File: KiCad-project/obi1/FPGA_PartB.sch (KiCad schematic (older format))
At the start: 10 parts, among them U3 XC6SLX16-FTG256

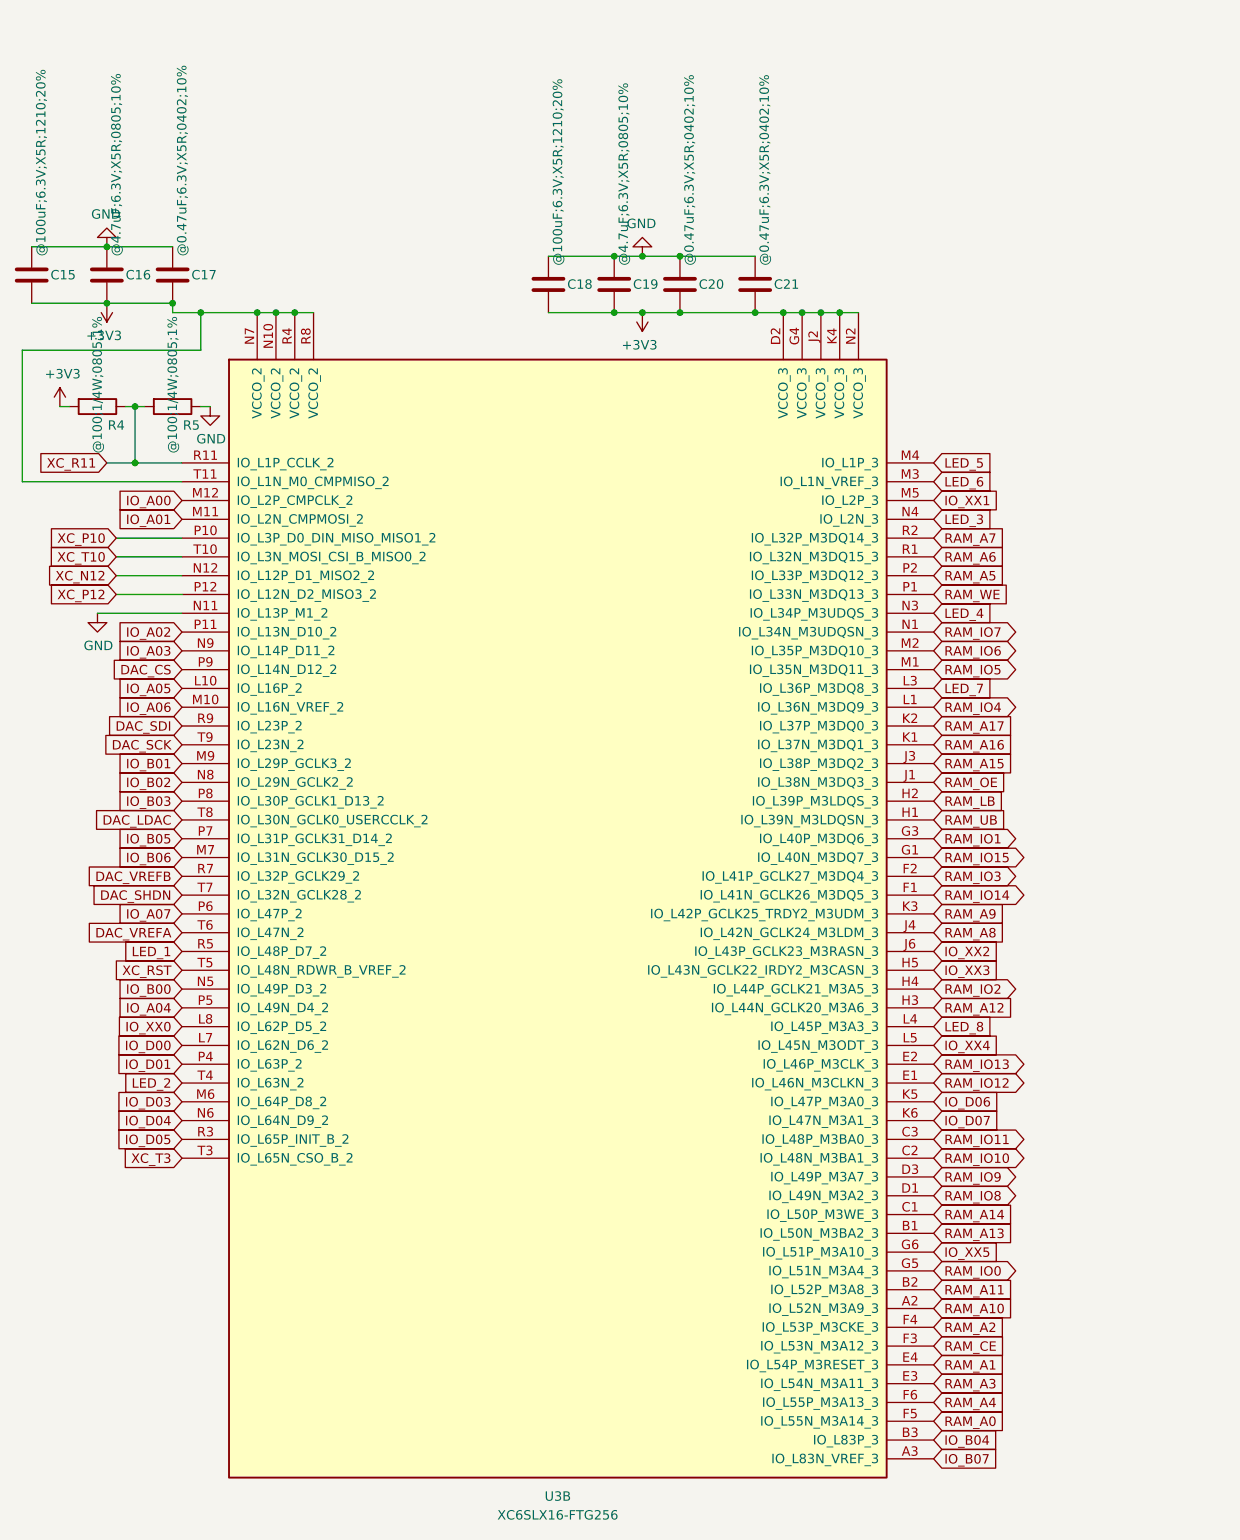
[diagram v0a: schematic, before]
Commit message: Resize board, change layout, re-route IO pins, new imu added
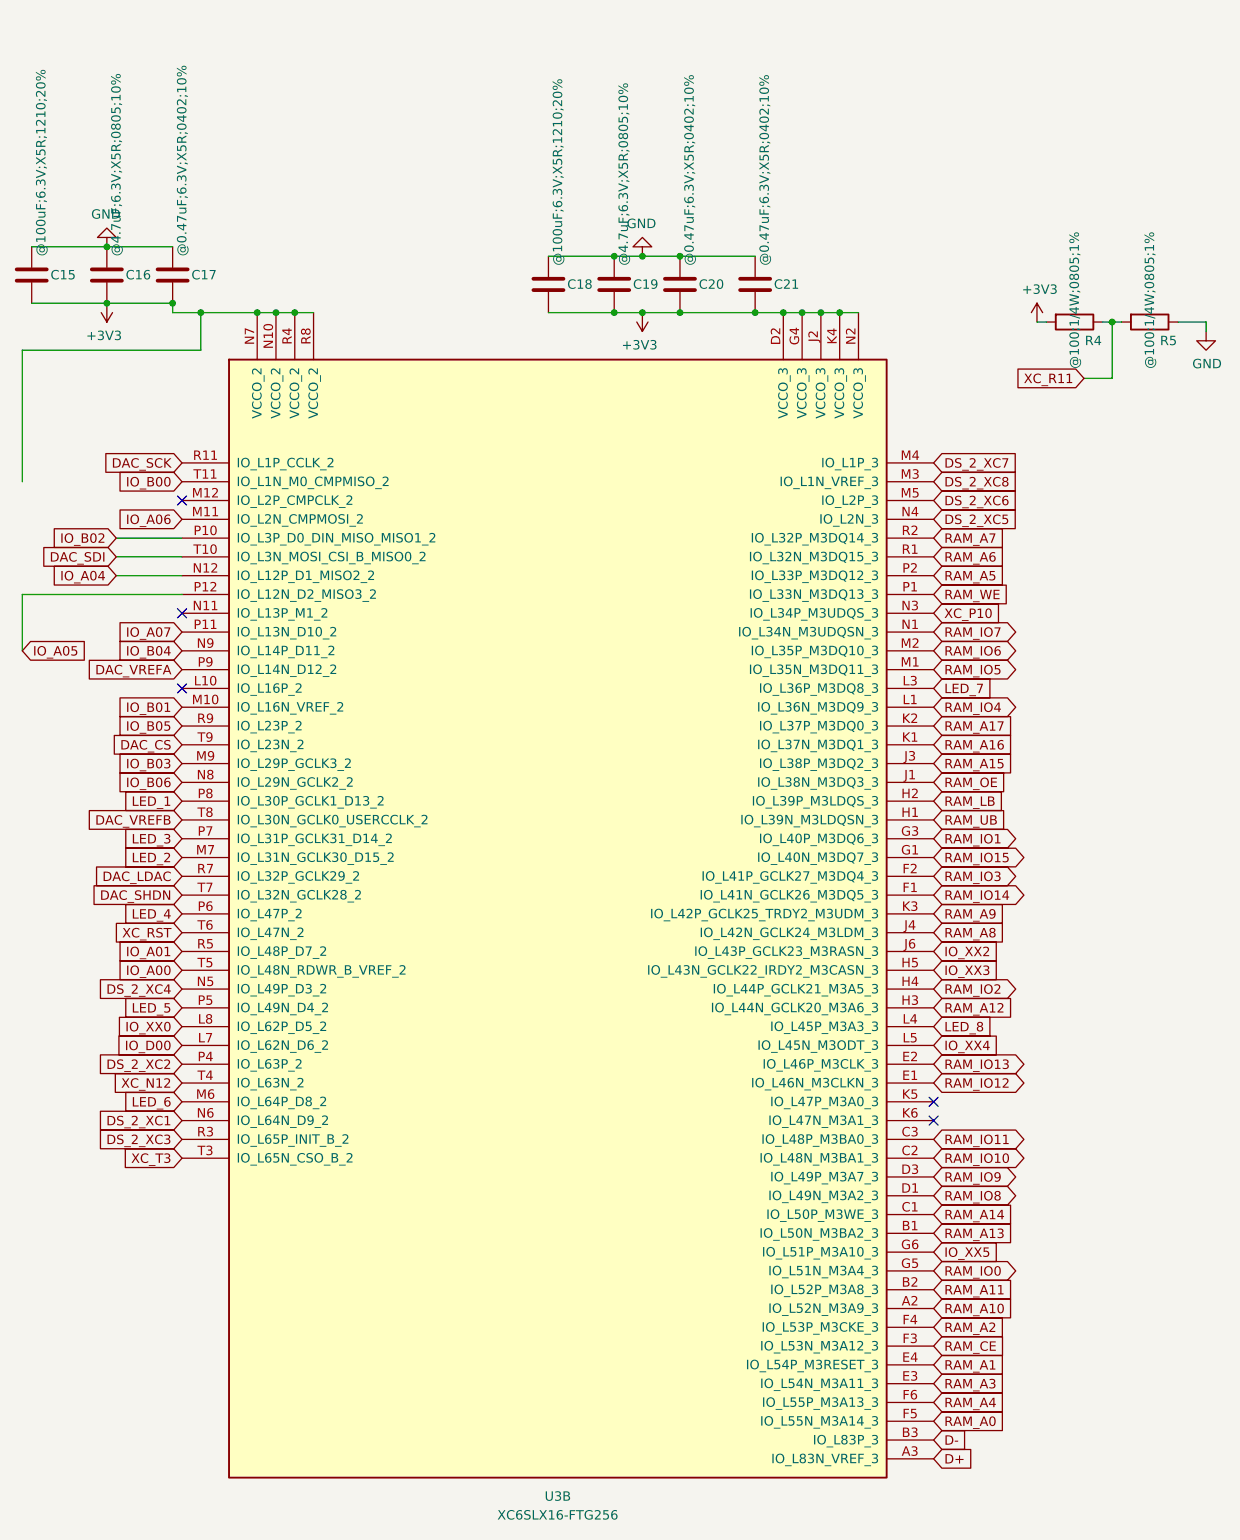
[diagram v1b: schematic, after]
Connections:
- net labels added: D+, D-, DS_2_XC1, DS_2_XC2, DS_2_XC3, DS_2_XC4, DS_2_XC5, DS_2_XC6, DS_2_XC7, DS_2_XC8
- net labels removed: IO_A02, IO_A03, IO_B07, IO_D01, IO_D03, IO_D04, IO_D05, IO_D06, IO_D07, IO_XX1, XC_P12, XC_T10
- wire segments 39 -> 38
- no-connect marks 0 -> 5
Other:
- moved on the sheet: R4, R5
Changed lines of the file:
@@
 Comment4 ""
 $EndDescr
-$Comp
-L FPGA_Xilinx_Spartan6:XC6SLX16-FTG256 U3
-U 2 1 5DA5D5E1
-P 3450 4150
-F 0 "U3" H 3450 950 50  0000 C CNN
-F 1 "XC6SLX16-FTG256" H 3450 850 50  0000 C CNN
-F 2 "Package_BGA:BGA-256_17.0x17.0mm_Layout16x16_P1.0mm_Ball0.5mm_Pad0.4mm_NSMD" H 3450 4150 50  0001 C CNN
-F 3 "" H 3450 4150 50  0000 C CNN
-	2    3450 4150
-	1    0    0    -1
-$EndComp
-Text GLabel 1050 1850 0    50   Input ~ 0
-XC_R11
-Text GLabel 1100 2250 0    50   Input ~ 0
+Text GLabel 5450 2650 2    50   Input ~ 0
 XC_P10
-Text GLabel 1100 2350 0    50   Input ~ 0
-XC_T10
-Text GLabel 1100 2450 0    50   Input ~ 0
+Text GLabel 1450 5150 0    50   Input ~ 0
 XC_N12
-Text GLabel 1100 2550 0    50   Input ~ 0
-XC_P12
-Wire Wire Line
-	1100 2550 1450 2550
 Wire Wire Line
 	1450 2350 1100 2350
@@
 Wire Wire Line
 	1450 2250 1100 2250
-Wire Wire Line
-	1450 1850 1200 1850
-$Comp
-L power:+3V3 #PWR023
-U 1 1 5D980361
-P 800 1550
-F 0 "#PWR023" H 800 1400 50  0001 C CNN
-F 1 "+3V3" H 815 1723 50  0000 C CNN
-F 2 "" H 800 1550 50  0001 C CNN
-F 3 "" H 800 1550 50  0001 C CNN
-	1    800  1550
-	1    0    0    -1
-$EndComp
-$Comp
-L Device:R R4
-U 1 1 5D981556
-P 1000 1550
-F 0 "R4" V 1100 1650 50  0000 C CNN
-F 1 "@100;1/4W;0805;1%" H 884 1550 50  0000 C CNN
-F 2 "Resistor_SMD:R_0805_2012Metric_Pad1.20x1.40mm_HandSolder" V 930 1550 50  0001 C CNN
-F 3 "~" H 1000 1550 50  0001 C CNN
-	1    1000 1550
-	0    1    1    0
-$EndComp
-$Comp
-L Device:R R5
-U 1 1 5D981903
-P 1400 1550
-F 0 "R5" V 1500 1650 50  0000 C CNN
-F 1 "@100;1/4W;0805;1%" H 1284 1550 50  0000 C CNN
-F 2 "Resistor_SMD:R_0805_2012Metric_Pad1.20x1.40mm_HandSolder" V 1330 1550 50  0001 C CNN
-F 3 "~" H 1400 1550 50  0001 C CNN
-	1    1400 1550
-	0    1    1    0
-$EndComp
-$Comp
-L power:GND #PWR027
-U 1 1 5D981CA2
-P 1600 1550
-F 0 "#PWR027" H 1600 1300 50  0001 C CNN
-F 1 "GND" H 1605 1377 50  0000 C CNN
-F 2 "" H 1600 1550 50  0001 C CNN
-F 3 "" H 1600 1550 50  0001 C CNN
-	1    1600 1550
-	1    0    0    -1
-$EndComp
-Wire Wire Line
-	1600 1550 1550 1550
-Wire Wire Line
-	1250 1550 1200 1550
-Wire Wire Line
-	800  1550 850  1550
-Wire Wire Line
-	1200 1850 1200 1550
-Connection ~ 1200 1850
-Wire Wire Line
-	1200 1850 1050 1850
-Connection ~ 1200 1550
-Wire Wire Line
-	1200 1550 1150 1550
-$Comp
-L power:GND #PWR024
-U 1 1 5D984152
-P 1000 2650
-F 0 "#PWR024" H 1000 2400 50  0001 C CNN
-F 1 "GND" H 1005 2477 50  0000 C CNN
-F 2 "" H 1000 2650 50  0001 C CNN
-F 3 "" H 1000 2650 50  0001 C CNN
-	1    1000 2650
-	1    0    0    -1
-$EndComp
-Wire Wire Line
-	1000 2650 1450 2650
-Wire Wire Line
-	2150 1050 2050 1050
-Connection ~ 1950 1050
-Wire Wire Line
-	1950 1050 1850 1050
-Connection ~ 2050 1050
-Wire Wire Line
-	2050 1050 1950 1050
 $Comp
 L Device:C C17
@@
 	1    0    0    -1
 $EndComp
-Wire Wire Line
-	5050 1050 4950 1050
 Connection ~ 3750 1050
 Wire Wire Line
@@
 Wire Wire Line
 	4500 1050 4100 1050
-Connection ~ 4650 1050
-Wire Wire Line
-	4650 1050 4500 1050
-Connection ~ 4750 1050
-Wire Wire Line
-	4750 1050 4650 1050
-Connection ~ 4850 1050
-Wire Wire Line
-	4850 1050 4750 1050
-Connection ~ 4950 1050
-Wire Wire Line
-	4950 1050 4850 1050
 Wire Wire Line
 	4500 750  4100 750
@@
 Wire Wire Line
 	1400 1050 1400 1000
-Connection ~ 1850 1050
 Text GLabel 1450 5550 0    50   Input ~ 0
 XC_T3
@@
 Text GLabel 5450 6350 2    50   Input ~ 0
 RAM_A10
-Text GLabel 1450 2750 0    50   Input ~ 0
-IO_A02
-Text GLabel 1450 2850 0    50   Input ~ 0
-IO_A03
-Text GLabel 1450 4750 0    50   Input ~ 0
-IO_A04
-Text GLabel 1450 3050 0    50   Input ~ 0
-IO_A05
-Text GLabel 1450 3150 0    50   Input ~ 0
-IO_A06
-Text GLabel 1450 4250 0    50   Input ~ 0
-IO_A07
-Text GLabel 1450 3450 0    50   Input ~ 0
-IO_B01
-Text GLabel 1450 3550 0    50   Input ~ 0
-IO_B02
-Text GLabel 1450 3650 0    50   Input ~ 0
-IO_B03
-Text GLabel 5450 7050 2    50   Input ~ 0
-IO_B04
-Text GLabel 1450 3850 0    50   Input ~ 0
-IO_B05
-Text GLabel 1450 3950 0    50   Input ~ 0
-IO_B06
-Text GLabel 5450 7150 2    50   Input ~ 0
-IO_B07
-Text GLabel 1450 2050 0    50   Input ~ 0
-IO_A00
-Text GLabel 1450 2150 0    50   Input ~ 0
-IO_A01
 Text GLabel 1450 4950 0    50   Input ~ 0
 IO_D00
-Text GLabel 1450 5050 0    50   Input ~ 0
-IO_D01
-Text GLabel 1450 4550 0    50   Input ~ 0
+Text GLabel 1450 4350 0    50   Input ~ 0
 XC_RST
+Text GLabel 1450 3850 0    50   Input ~ 0
+LED_3
+Text GLabel 1450 4750 0    50   Input ~ 0
+LED_5
 Text GLabel 1450 5250 0    50   Input ~ 0
-IO_D03
-Text GLabel 1450 5350 0    50   Input ~ 0
-IO_D04
-Text GLabel 1450 5450 0    50   Input ~ 0
-IO_D05
-Text GLabel 5450 5250 2    50   Input ~ 0
-IO_D06
-Text GLabel 5450 5350 2    50   Input ~ 0
-IO_D07
-Text GLabel 1450 4450 0    50   Input ~ 0
-LED_1
-Text GLabel 1450 5150 0    50   Input ~ 0
-LED_2
-Text GLabel 5450 2150 2    50   Input ~ 0
-LED_3
-Text GLabel 5450 2650 2    50   Input ~ 0
-LED_4
-Text GLabel 5450 1850 2    50   Input ~ 0
-LED_5
-Text GLabel 5450 1950 2    50   Input ~ 0
 LED_6
 Text GLabel 5450 3050 2    50   Input ~ 0
@@
 Text GLabel 5450 4850 2    50   Input ~ 0
 LED_8
-Text GLabel 5450 2050 2    50   Input ~ 0
-IO_XX1
 Text GLabel 5450 4450 2    50   Input ~ 0
 IO_XX2
@@
 Wire Wire Line
 	1550 1250 1550 1050
-Wire Wire Line
-	600  1950 1450 1950
 Connection ~ 1550 1050
-Wire Wire Line
-	1550 1050 1850 1050
 Text GLabel 5450 4750 2    50   Input ~ 0
 RAM_A12
 Text GLabel 5450 6150 2    50   BiDi ~ 0
 RAM_IO0
+Text GLabel 1450 3350 0    50   Input ~ 0
+DAC_CS
+Text GLabel 1450 1850 0    50   Input ~ 0
+DAC_SCK
 Text GLabel 1450 2950 0    50   Input ~ 0
-DAC_CS
-Text GLabel 1450 3350 0    50   Input ~ 0
-DAC_SCK
-Text GLabel 1450 3250 0    50   Input ~ 0
+DAC_VREFA
+Text GLabel 1450 3750 0    50   Input ~ 0
+DAC_VREFB
+Text GLabel 1450 4850 0    50   Input ~ 0
+IO_XX0
+Text GLabel 1450 4250 0    50   Input ~ 0
+LED_4
+Text GLabel 1450 3950 0    50   Input ~ 0
+LED_2
+Text GLabel 1450 3650 0    50   Input ~ 0
+LED_1
+Text GLabel 1100 2350 0    50   Input ~ 0
 DAC_SDI
-Text GLabel 1450 4350 0    50   Input ~ 0
-DAC_VREFA
+Wire Wire Line
+	600  2550 600  2850
+Wire Wire Line
+	600  2550 1450 2550
+Wire Wire Line
+	5050 1050 4950 1050
+Connection ~ 4950 1050
+Wire Wire Line
+	4950 1050 4850 1050
+Connection ~ 4850 1050
+Wire Wire Line
+	4850 1050 4750 1050
+Connection ~ 4750 1050
+Wire Wire Line
+	4750 1050 4650 1050
+Wire Wire Line
+	4650 1050 4500 1050
+Connection ~ 4650 1050
+Wire Wire Line
+	2150 1050 2050 1050
+Connection ~ 2050 1050
+Wire Wire Line
+	2050 1050 1950 1050
+Connection ~ 1950 1050
+Wire Wire Line
+	1550 1050 1850 1050
+Wire Wire Line
+	1950 1050 1850 1050
+Connection ~ 1850 1050
+$Comp
+L FPGA_Xilinx_Spartan6:XC6SLX16-FTG256 U3
+U 2 1 5DA5D5E1
+P 3450 4150
+F 0 "U3" H 3450 950 50  0000 C CNN
+F 1 "XC6SLX16-FTG256" H 3450 850 50  0000 C CNN
+F 2 "Package_BGA:BGA-256_17.0x17.0mm_Layout16x16_P1.0mm_Ball0.5mm_Pad0.4mm_NSMD" H 3450 4150 50  0001 C CNN
+F 3 "" H 3450 4150 50  0000 C CNN
+	2    3450 4150
+	1    0    0    -1
+$EndComp
+Text GLabel 6250 1400 0    50   Input ~ 0
+XC_R11
+$Comp
+L power:+3V3 #PWR023
+U 1 1 5D980361
+P 6000 1100
+F 0 "#PWR023" H 6000 950 50  0001 C CNN
+F 1 "+3V3" H 6015 1273 50  0000 C CNN
+F 2 "" H 6000 1100 50  0001 C CNN
+F 3 "" H 6000 1100 50  0001 C CNN
+	1    6000 1100
+	1    0    0    -1
+$EndComp
+$Comp
+L Device:R R4
+U 1 1 5D981556
+P 6200 1100
+F 0 "R4" V 6300 1200 50  0000 C CNN
+F 1 "@100;1/4W;0805;1%" H 6084 1100 50  0000 C CNN
+F 2 "Resistor_SMD:R_0805_2012Metric_Pad1.20x1.40mm_HandSolder" V 6130 1100 50  0001 C CNN
+F 3 "~" H 6200 1100 50  0001 C CNN
+	1    6200 1100
+	0    1    1    0
+$EndComp
+$Comp
+L Device:R R5
+U 1 1 5D981903
+P 6600 1100
+F 0 "R5" V 6700 1200 50  0000 C CNN
+F 1 "@100;1/4W;0805;1%" H 6484 1100 50  0000 C CNN
+F 2 "Resistor_SMD:R_0805_2012Metric_Pad1.20x1.40mm_HandSolder" V 6530 1100 50  0001 C CNN
+F 3 "~" H 6600 1100 50  0001 C CNN
+	1    6600 1100
+	0    1    1    0
+$EndComp
+Wire Wire Line
+	6450 1100 6400 1100
+Wire Wire Line
+	6000 1100 6050 1100
+Wire Wire Line
+	6400 1400 6400 1100
+Wire Wire Line
+	6400 1400 6250 1400
+Connection ~ 6400 1100
+Wire Wire Line
+	6400 1100 6350 1100
+$Comp
+L power:GND #PWR027
+U 1 1 5D981CA2
+P 6900 1150
+F 0 "#PWR027" H 6900 900 50  0001 C CNN
+F 1 "GND" H 6905 977 50  0000 C CNN
+F 2 "" H 6900 1150 50  0001 C CNN
+F 3 "" H 6900 1150 50  0001 C CNN
+	1    6900 1150
+	1    0    0    -1
+$EndComp
+Wire Wire Line
+	6750 1100 6900 1100
+Wire Wire Line
+	6900 1100 6900 1150
 Text GLabel 1450 4050 0    50   Input ~ 0
-DAC_VREFB
+DAC_LDAC
 Text GLabel 1450 4150 0    50   Input ~ 0
 DAC_SHDN
-Text GLabel 1450 3750 0    50   Input ~ 0
-DAC_LDAC
-Text GLabel 1450 4850 0    50   Input ~ 0
-IO_XX0
+Text GLabel 5450 7150 2    50   Input ~ 0
+D+
+Text GLabel 5450 7050 2    50   Input ~ 0
+D-
+Text GLabel 1450 5350 0    50   Input ~ 0
+DS_2_XC1
+Text GLabel 1450 5050 0    50   Input ~ 0
+DS_2_XC2
+Text GLabel 1450 5450 0    50   Input ~ 0
+DS_2_XC3
 Text GLabel 1450 4650 0    50   Input ~ 0
+DS_2_XC4
+Text GLabel 5450 2150 2    50   Input ~ 0
+DS_2_XC5
+Text GLabel 5450 2050 2    50   Input ~ 0
+DS_2_XC6
+Text GLabel 5450 1850 2    50   Input ~ 0
+DS_2_XC7
+Text GLabel 5450 1950 2    50   Input ~ 0
+DS_2_XC8
+Text GLabel 600  2850 2    50   Input ~ 0
+IO_A05
+Text GLabel 1450 2150 0    50   Input ~ 0
+IO_A06
+Text GLabel 1450 4450 0    50   Input ~ 0
+IO_A01
+Text GLabel 1450 4550 0    50   Input ~ 0
+IO_A00
+Text GLabel 1100 2450 0    50   Input ~ 0
+IO_A04
+Text GLabel 1450 2750 0    50   Input ~ 0
+IO_A07
+Text GLabel 1450 3150 0    50   Input ~ 0
+IO_B01
+Text GLabel 1450 3550 0    50   Input ~ 0
+IO_B06
+Text GLabel 1450 2850 0    50   Input ~ 0
+IO_B04
+Text GLabel 1100 2250 0    50   Input ~ 0
+IO_B02
+Text GLabel 1450 3450 0    50   Input ~ 0
+IO_B03
+Text GLabel 1450 1950 0    50   Input ~ 0
 IO_B00
+Text GLabel 1450 3250 0    50   Input ~ 0
+IO_B05
+NoConn ~ 1450 2050
+NoConn ~ 1450 2650
+NoConn ~ 1450 3050
+NoConn ~ 5450 5250
+NoConn ~ 5450 5350
 $EndSCHEMATC
